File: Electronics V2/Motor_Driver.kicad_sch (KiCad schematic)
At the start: 11 parts

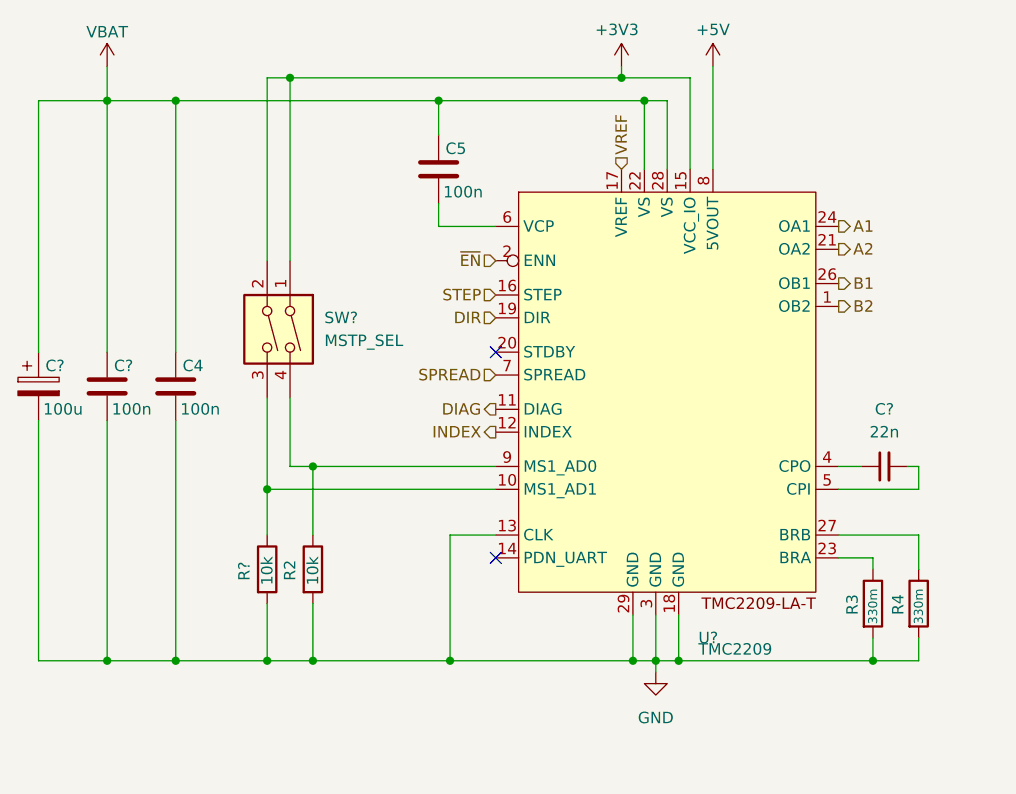
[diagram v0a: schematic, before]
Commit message: needs footprints
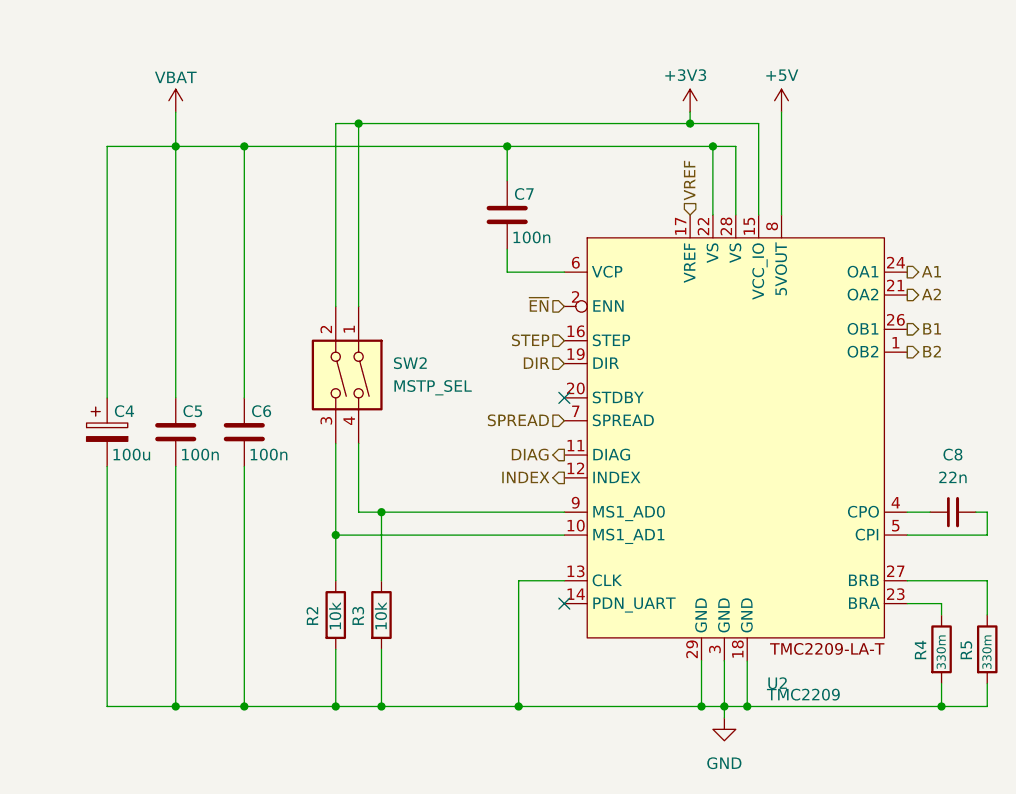
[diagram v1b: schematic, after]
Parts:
- removed C4, C?: 100n, symbol Device:C
- removed C?: 100u, symbol Device:C_Polarized
- removed C?: 22n, symbol Device:C_Small
- removed R?: 10k, symbol Device:R
- removed SW?: MSTP_SEL, symbol Switch:SW_DIP_x02
- removed U?: TMC2209, Package_DFN_QFN:QFN-28-1EP_5x5mm_P0.5mm_EP3.75x3.75mm, symbol TMC2209-LA-T:TMC2209-LA-T
- added C4: 100u, symbol Device:C_Polarized
- added C6, C7: 100n, symbol Device:C
- added C8: 22n, symbol Device:C_Small
- added R5: 330m, symbol Device:R
- added SW2: MSTP_SEL, symbol Switch:SW_DIP_x02
- added U2: TMC2209, Package_DFN_QFN:QFN-28-1EP_5x5mm_P0.5mm_EP3.75x3.75mm, symbol TMC2209-LA-T:TMC2209-LA-T
- R3: value 330m -> 10k
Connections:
- net +3V3: now also SW2.1, SW2.2, U2.15 (VCC_IO)
- net +5V: now also U2.8 (5VOUT)
- net A1: now also U2.24 (OA1)
- net A2: now also U2.21 (OA2)
- net B1: now also U2.26 (OB1)
- net B2: now also U2.1 (OB2)
- net DIAG: now also U2.11 (DIAG)
- net DIR: now also U2.19 (DIR)
- net GND: now also C5.2, C4.2, C6.2, R5.2, U2.13 (CLK), U2.18 (GND), U2.29 (GND), U2.3 (GND)
- net INDEX: now also U2.12 (INDEX)
- net SPREAD: now also U2.7 (SPREAD)
- net STEP: now also U2.16 (STEP)
- net VBAT: now also C4.1, C6.1, C7.1, U2.22 (VS), U2.28 (VS)
- net VREF: now also U2.17 (VREF)
- net ~{EN}: now also U2.2 (ENN)
- net at R3.1: now also SW2.4, U2.9 (MS1_AD0)
- net at R4.1: now also U2.23 (BRA)
- net at R2.1: now also SW2.3, U2.10 (MS1_AD1)
- new net: C8.1, U2.4 (CPO)
- new net: C8.2, U2.5 (CPI)
- new net: C7.2, U2.6 (VCP)
- new net: R5.1, U2.27 (BRB)

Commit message: footprints
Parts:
- C4: footprint (none) -> Capacitor_SMD:C_0805_2012Metric
- C5, C6, C7: footprint (none) -> Capacitor_SMD:C_0603_1608Metric
- C8: footprint (none) -> Capacitor_SMD:C_1206_3216Metric
- R2, R3, R4, R5: footprint (none) -> Resistor_SMD:R_0603_1608Metric
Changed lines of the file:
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@@
 			)
 		)
-		(property "Footprint" ""
+		(property "Footprint" "Resistor_SMD:R_0603_1608Metric"
 			(at 132.842 123.19 90)
 			(effects
@@
 			)
 		)
-		(property "Footprint" ""
+		(property "Footprint" "Capacitor_SMD:C_0603_1608Metric"
 			(at 125.4252 106.68 0)
 			(effects
@@
 			)
 		)
-		(property "Footprint" ""
+		(property "Footprint" "Capacitor_SMD:C_0603_1608Metric"
 			(at 117.8052 106.68 0)
 			(effects
@@
 			)
 		)
-		(property "Footprint" ""
+		(property "Footprint" "Resistor_SMD:R_0603_1608Metric"
 			(at 200.152 127 90)
 			(effects
@@
 			)
 		)
-		(property "Footprint" ""
+		(property "Footprint" "Capacitor_SMD:C_1206_3216Metric"
 			(at 203.2 111.76 0)
 			(effects
@@
 			)
 		)
-		(property "Footprint" ""
+		(property "Footprint" "Capacitor_SMD:C_0603_1608Metric"
 			(at 154.6352 82.55 0)
 			(effects
@@
 			)
 		)
-		(property "Footprint" ""
+		(property "Footprint" "Resistor_SMD:R_0603_1608Metric"
 			(at 205.232 127 90)
 			(effects
@@
 			)
 		)
-		(property "Footprint" ""
+		(property "Footprint" "Resistor_SMD:R_0603_1608Metric"
 			(at 137.922 123.19 90)
 			(effects
@@
 			)
 		)
-		(property "Footprint" ""
+		(property "Footprint" "Capacitor_SMD:C_0805_2012Metric"
 			(at 110.1852 106.68 0)
 			(effects

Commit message: new board, needs usb, buttons, power, esd protection, transients, etc
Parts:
- C8: footprint Capacitor_SMD:C_1206_3216Metric -> Capacitor_SMD:C_0603_1608Metric
- SW2: footprint (none) -> Button_Switch_SMD:SW_DIP_SPSTx02_Slide_6.7x6.64mm_W6.73mm_P2.54mm_LowProfile_JPin
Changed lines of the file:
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@@
 			)
 		)
-		(property "Footprint" ""
+		(property "Footprint" "Button_Switch_SMD:SW_DIP_SPSTx02_Slide_6.7x6.64mm_W6.73mm_P2.54mm_LowProfile_JPin"
 			(at 134.62 96.52 0)
 			(effects
@@
 			)
 		)
-		(property "Footprint" "Capacitor_SMD:C_1206_3216Metric"
+		(property "Footprint" "Capacitor_SMD:C_0603_1608Metric"
 			(at 203.2 111.76 0)
 			(effects

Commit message: ready ro route
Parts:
- C4: footprint Capacitor_SMD:C_0805_2012Metric -> Capacitor_Tantalum_SMD:CP_EIA-7343-30_AVX-N
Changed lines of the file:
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@@
 			)
 		)
-		(property "Footprint" "Capacitor_SMD:C_0805_2012Metric"
+		(property "Footprint" "Capacitor_Tantalum_SMD:CP_EIA-7343-30_AVX-N"
 			(at 110.1852 106.68 0)
 			(effects

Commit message: placing done
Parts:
- removed SW2: MSTP_SEL, Button_Switch_SMD:SW_DIP_SPSTx02_Slide_6.7x6.64mm_W6.73mm_P2.54mm_LowProfile_JPin, symbol Switch:SW_DIP_x02
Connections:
- net MS1_AD1: now reaches R2.1, U2.10 (MS1_AD1)
- net MS1_AD0: now reaches R3.1, U2.9 (MS1_AD0)
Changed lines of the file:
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@@
-	)
-	(junction
-		(at 137.16 68.58)
-		(diameter 0)
-		(color 0 0 0 0)
 	)
 	(junction
@@
 	)
 	(junction
-		(at 173.99 68.58)
-		(diameter 0)
-		(color 0 0 0 0)
-	)
-	(junction
 		(at 180.34 133.35)
 		(diameter 0)
@@
 	(wire
 		(pts
-			(xy 134.62 68.58) (xy 134.62 88.9)
-		)
-		(stroke
-			(width 0)
-			(type default)
-		)
-	)
-	(wire
-		(pts
 			(xy 124.46 99.06) (xy 124.46 71.12)
 		)
@@
 	(wire
 		(pts
-			(xy 137.16 68.58) (xy 173.99 68.58)
-		)
-		(stroke
-			(width 0)
-			(type default)
-		)
-	)
-	(wire
-		(pts
 			(xy 179.07 78.74) (xy 179.07 71.12)
 		)
@@
 	(wire
 		(pts
-			(xy 173.99 67.31) (xy 173.99 68.58)
-		)
-		(stroke
-			(width 0)
-			(type default)
-		)
-	)
-	(wire
-		(pts
 			(xy 134.62 127) (xy 134.62 133.35)
 		)
@@
 	(wire
 		(pts
-			(xy 137.16 68.58) (xy 134.62 68.58)
-		)
-		(stroke
-			(width 0)
-			(type default)
-		)
-	)
-	(wire
-		(pts
 			(xy 137.16 111.76) (xy 139.7 111.76)
 		)
@@
 	(wire
 		(pts
-			(xy 181.61 68.58) (xy 181.61 78.74)
+			(xy 181.61 67.31) (xy 181.61 78.74)
 		)
 		(stroke
@@
 	(wire
 		(pts
-			(xy 137.16 68.58) (xy 137.16 88.9)
-		)
-		(stroke
-			(width 0)
-			(type default)
-		)
-	)
-	(wire
-		(pts
 			(xy 116.84 133.35) (xy 124.46 133.35)
 		)
@@
 		(pts
 			(xy 116.84 71.12) (xy 109.22 71.12)
-		)
-		(stroke
-			(width 0)
-			(type default)
-		)
-	)
-	(wire
-		(pts
-			(xy 173.99 68.58) (xy 181.61 68.58)
 		)
 		(stroke
@@
 		)
 	)
+	(hierarchical_label "MS1_AD1"
+		(shape input)
+		(at 134.62 104.14 90)
+		(effects
+			(font
+				(size 1.27 1.27)
+			)
+			(justify left)
+		)
+	)
 	(hierarchical_label "B1"
 		(shape output)
@@
 		)
 	)
+	(hierarchical_label "MS1_AD0"
+		(shape input)
+		(at 137.16 104.14 90)
+		(effects
+			(font
+				(size 1.27 1.27)
+			)
+			(justify left)
+		)
+	)
 	(symbol
 		(lib_id "power:+3V3")
-		(at 173.99 67.31 0)
+		(at 181.61 67.31 0)
 		(unit 1)
 		(exclude_from_sim no)
@@
 		(dnp no)
 		(property "Reference" "#PWR06"
-			(at 173.99 71.12 0)
+			(at 181.61 71.12 0)
 			(effects
 				(font
@@
 		)
 		(property "Value" "+3V3"
-			(at 173.482 63.246 0)
+			(at 179.324 63.246 0)
 			(effects
 				(font
@@
 		)
 		(property "Footprint" ""
-			(at 173.99 67.31 0)
+			(at 181.61 67.31 0)
 			(effects
 				(font
@@
 		)
 		(property "Datasheet" ""
-			(at 173.99 67.31 0)
+			(at 181.61 67.31 0)
 			(effects
 				(font
@@
 		)
 		(property "Description" "Power symbol creates a global label with name \"+3V3\""
-			(at 173.99 67.31 0)
+			(at 181.61 67.31 0)
 			(effects
 				(font
@@
 				(path "/fb299ee1-36f2-498d-9da8-1c8d846ea71b/985db7d4-b2c2-4df1-b468-45cc87e10652"
 					(reference "#PWR024")
-					(unit 1)
-				)
-			)
-		)
-	)
-	(symbol
-		(lib_id "Switch:SW_DIP_x02")
-		(at 134.62 96.52 270)
-		(unit 1)
-		(exclude_from_sim no)
-		(in_bom yes)
-		(on_board yes)
-		(dnp no)
-		(fields_autoplaced yes)
-		(property "Reference" "SW2"
-			(at 140.97 95.2499 90)
-			(effects
-				(font
-					(size 1.27 1.27)
-				)
-				(justify left)
-			)
-		)
-		(property "Value" "MSTP_SEL"
-			(at 140.97 97.7899 90)
-			(effects
-				(font
-					(size 1.27 1.27)
-				)
-				(justify left)
-			)
-		)
-		(property "Footprint" "Button_Switch_SMD:SW_DIP_SPSTx02_Slide_6.7x6.64mm_W6.73mm_P2.54mm_LowProfile_JPin"
-			(at 134.62 96.52 0)
-			(effects
-				(font
-					(size 1.27 1.27)
-				)
-				(hide yes)
-			)
-		)
-		(property "Datasheet" "~"
-			(at 134.62 96.52 0)
-			(effects
-				(font
-					(size 1.27 1.27)
-				)
-				(hide yes)
-			)
-		)
-		(property "Description" "2x DIP Switch, Single Pole Single Throw (SPST) switch, small symbol"
-			(at 134.62 96.52 0)
-			(effects
-				(font
-					(size 1.27 1.27)
-				)
-				(hide yes)
-			)
-		)
-		(pin "3"
-		)
-		(pin "1"
-		)
-		(pin "2"
-		)
-		(pin "4"
-		)
-		(instances
-			(project "Electronics V2"
-				(path "/fb299ee1-36f2-498d-9da8-1c8d846ea71b/0f841784-954e-46c8-b4bb-eac4b26f073d"
-					(reference "SW2")
-					(unit 1)
-				)
-				(path "/fb299ee1-36f2-498d-9da8-1c8d846ea71b/985db7d4-b2c2-4df1-b468-45cc87e10652"
-					(reference "SW9")
 					(unit 1)
 				)
@@
 		)
 		(property "Value" "+5V"
-			(at 184.15 63.246 0)
-			(effects
-				(font
+			(at 185.674 63.246 0)
+			(effects
+				(font

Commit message: finish routing jit
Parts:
- removed R2, R3: 10k, Resistor_SMD:R_0603_1608Metric, symbol Device:R
